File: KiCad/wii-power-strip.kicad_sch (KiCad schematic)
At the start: 11 parts, among them J1 Power

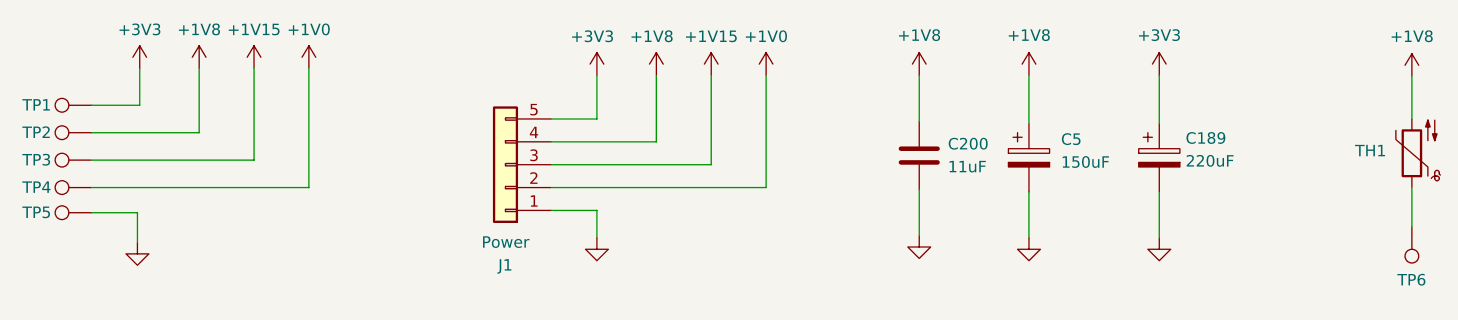
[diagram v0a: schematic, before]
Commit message: Left facing, 6-pin power connector
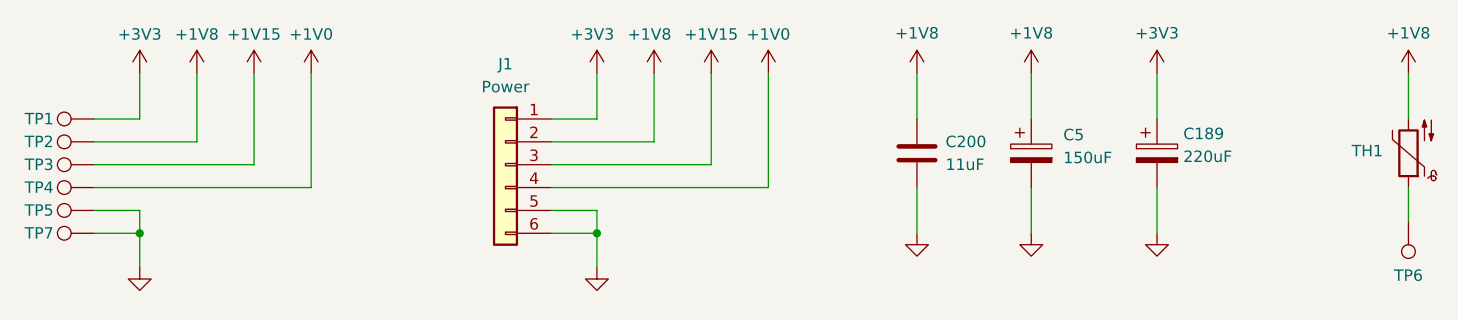
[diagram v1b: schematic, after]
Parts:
- added TP7: GND, project-footprints:TestPoint_Pad_3x1.0mm, symbol Connector:TestPoint
- C200: footprint (none) -> Capacitor_SMD:C_0805_2012Metric
- J1: footprint project-footprints:5040500591 -> project-footprints:504050-0691; symbol Connector_Generic:Conn_01x05 -> Connector_Generic:Conn_01x06
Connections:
- net +1V0: now also J1.4 (Pin_4); no longer J1.2 (Pin_2)
- net +1V8: now also J1.2 (Pin_2); no longer J1.4 (Pin_4)
- net +3V3: now also J1.1 (Pin_1); no longer J1.5 (Pin_5)
- net GND: now also J1.5 (Pin_5), J1.6 (Pin_6), TP7.1; no longer J1.1 (Pin_1)
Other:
- moved on the sheet: C189, C5, TP1, TP2, TP3, TP6

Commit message: Add castellated edges to voltage connections
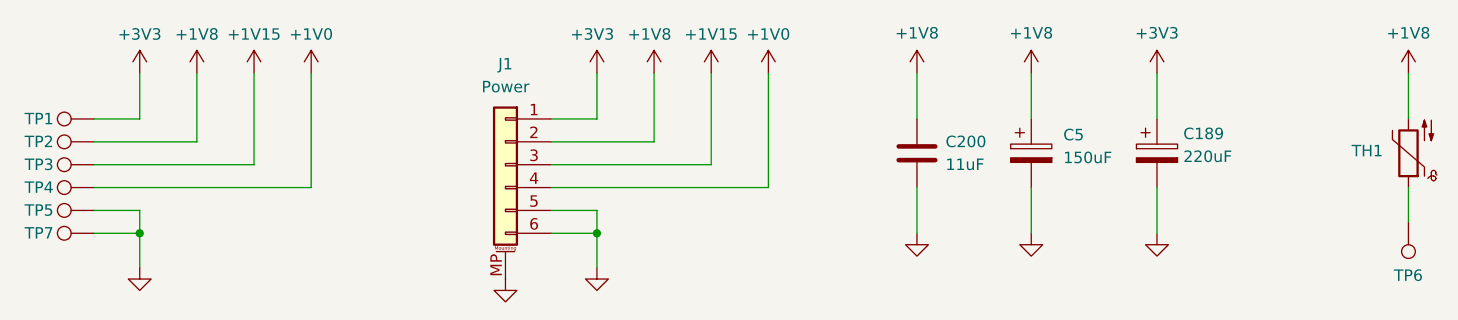
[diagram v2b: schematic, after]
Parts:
- J1: symbol Connector_Generic:Conn_01x06 -> Connector_Generic_MountingPin:Conn_01x06_MountingPin
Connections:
- net GND: now also J1.MP (MountPin)
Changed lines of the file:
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@@
 (kicad_sch
-	(version 20231120)
+	(version 20240417)
 	(generator "eeschema")
-	(generator_version "8.0")
+	(generator_version "8.99")
 	(paper "A4")
 	(junction
@@
 	)
 	(symbol
+		(lib_id "power:GND")
+		(at 118.11 110.49 0)
+		(unit 1)
+		(exclude_from_sim no)
+		(in_bom yes)
+		(on_board yes)
+		(dnp no)
+		(fields_autoplaced yes)
+		(property "Reference" "#PWR012"
+			(at 118.11 116.84 0)
+			(effects
+				(font
+					(size 1.27 1.27)
+				)
+				(hide yes)
+			)
+		)
+		(property "Value" "GND"
+			(at 118.11 115.57 0)
+			(effects
+				(font
+					(size 1.27 1.27)
+				)
+				(hide yes)
+			)
+		)
+		(property "Footprint" ""
+			(at 118.11 110.49 0)
+			(effects
+				(font
+					(size 1.27 1.27)
+				)
+				(hide yes)
+			)
+		)
+		(property "Datasheet" ""
+			(at 118.11 110.49 0)
+			(effects
+				(font
+					(size 1.27 1.27)
+				)
+				(hide yes)
+			)
+		)
+		(property "Description" ""
+			(at 118.11 110.49 0)
+			(effects
+				(font
+					(size 1.27 1.27)
+				)
+				(hide yes)
+			)
+		)
+		(property "MPN" ""
+			(at 118.11 110.49 0)
+			(effects
+				(font
+					(size 1.27 1.27)
+				)
+				(hide yes)
+			)
+		)
+		(property "Digi-Key Part #" ""
+			(at 118.11 110.49 0)
+			(effects
+				(font
+					(size 1.27 1.27)
+				)
+				(hide yes)
+			)
+		)
+		(pin "1"
+		)
+		(instances
+			(project "wii-power-strip"
+				(path "/f96ace2f-3864-49e4-b189-00e9bd1a19d1"
+					(reference "#PWR012")
+					(unit 1)
+				)
+			)
+		)
+	)
+	(symbol
 		(lib_id "power:+1V8")
 		(at 83.82 87.63 0)
@@
 	)
 	(symbol
-		(lib_id "Connector_Generic:Conn_01x06")
+		(lib_id "Connector_Generic_MountingPin:Conn_01x06_MountingPin")
 		(at 118.11 97.79 0)
 		(mirror y)
@@
 			)
 		)
-		(property "Description" "Generic connector, single row, 01x06, script generated (kicad-library-utils/schlib/autogen/connector/)"
+		(property "Description" "Generic connectable mounting pin connector, single row, 01x06, script generated (kicad-library-utils/schlib/autogen/connector/)"
 			(at 118.11 97.79 0)
 			(effects
@@
 		(pin "6"
 		)
-		(instances
+		(pin "MP"
+		)
+		(instances
